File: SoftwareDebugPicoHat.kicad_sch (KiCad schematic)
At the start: 14 parts, among them J1 35362-0950, J2 Conn_Coaxial, J3 USB_C_Receptacle_USB2.0_14P, J4 Conn_Coaxial, J5 Conn_01x04_Pin, U1 RFM98PW, U3 LORA1280F27-TCXO

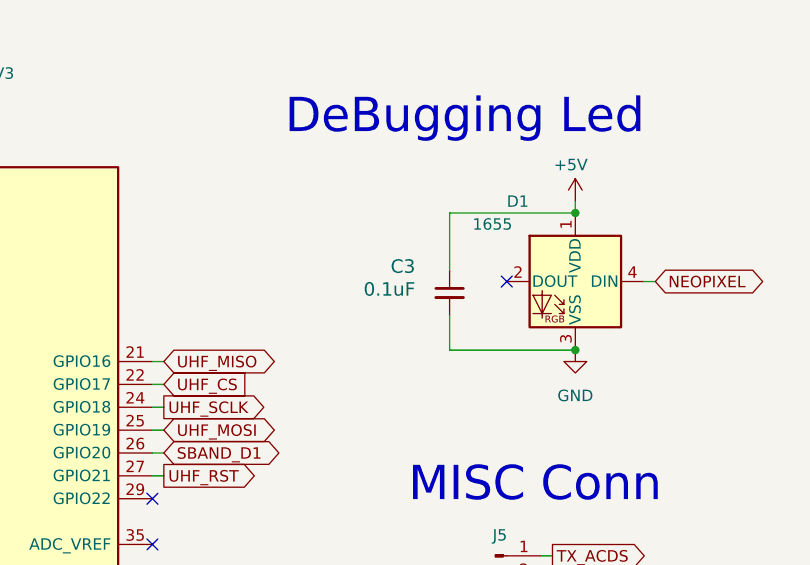
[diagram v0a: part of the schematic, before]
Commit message: Removed UBC and TCXO-EN Pullup resistor
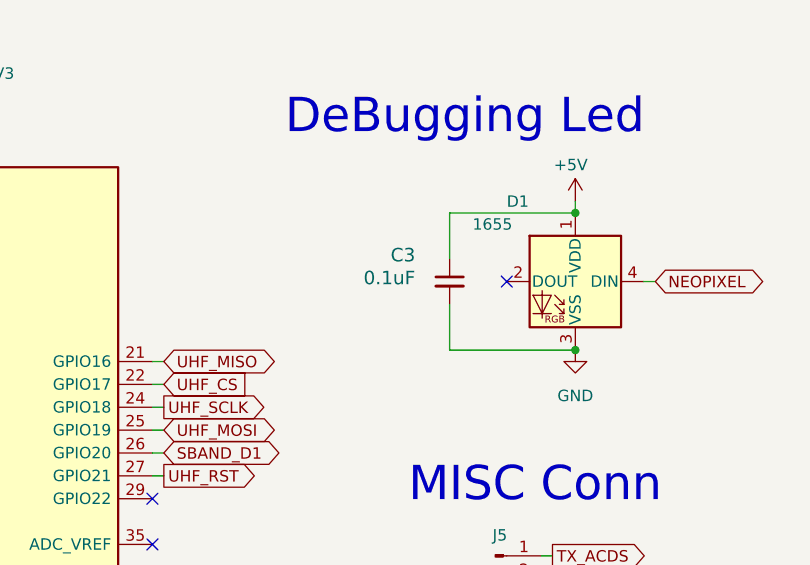
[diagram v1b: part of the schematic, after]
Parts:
- R1, R2: footprint (none) -> Resistor_SMD:R_0603_1608Metric
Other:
- moved on the sheet: C3
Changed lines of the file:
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@@
 	(wire
 		(pts
-			(xy 111.76 46.99) (xy 111.76 50.8)
+			(xy 111.76 45.72) (xy 111.76 50.8)
 		)
 		(stroke
@@
 	(wire
 		(pts
-			(xy 111.76 35.56) (xy 111.76 41.91)
+			(xy 111.76 35.56) (xy 111.76 40.64)
 		)
 		(stroke
@@
 	(symbol
 		(lib_id "Device:C_Small")
-		(at 111.76 44.45 0)
+		(at 111.76 43.18 0)
 		(unit 1)
 		(exclude_from_sim no)
@@
 		(dnp no)
 		(property "Reference" "C3"
-			(at 107.95 40.64 0)
+			(at 107.95 39.37 0)
 			(effects
 				(font
@@
 		)
 		(property "Value" "0.1uF"
-			(at 107.95 43.18 0)
+			(at 107.95 41.91 0)
 			(effects
 				(font
@@
 		)
 		(property "Footprint" "Capacitor_SMD:C_0603_1608Metric"
-			(at 111.76 44.45 0)
+			(at 111.76 43.18 0)
 			(effects
 				(font
@@
 		)
 		(property "Datasheet" "~"
-			(at 111.76 44.45 0)
+			(at 111.76 43.18 0)
 			(effects
 				(font
@@
 		)
 		(property "Description" "Unpolarized capacitor, small symbol"
-			(at 111.76 44.45 0)
+			(at 111.76 43.18 0)
 			(effects
 				(font
@@
 			)
 		)
-		(property "Footprint" ""
+		(property "Footprint" "Resistor_SMD:R_0603_1608Metric"
 			(at 55.88 135.89 0)
 			(effects
@@
 			)
 		)
-		(property "Footprint" ""
+		(property "Footprint" "Resistor_SMD:R_0603_1608Metric"
 			(at 59.69 133.35 0)
 			(effects

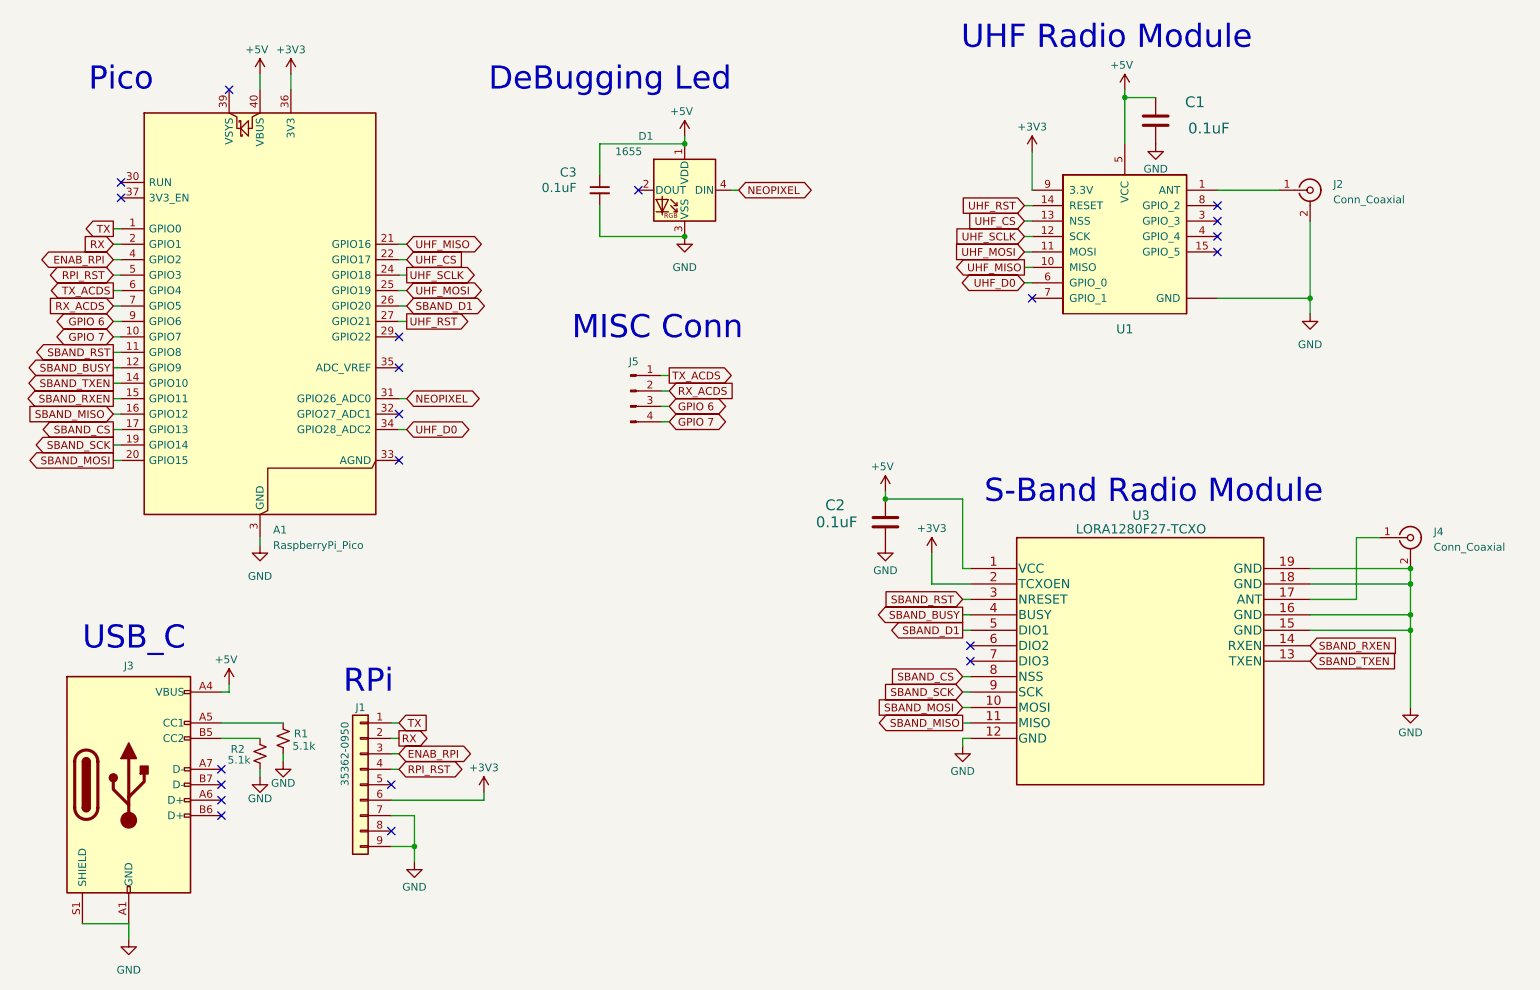
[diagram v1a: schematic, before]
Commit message: FIxed Caps
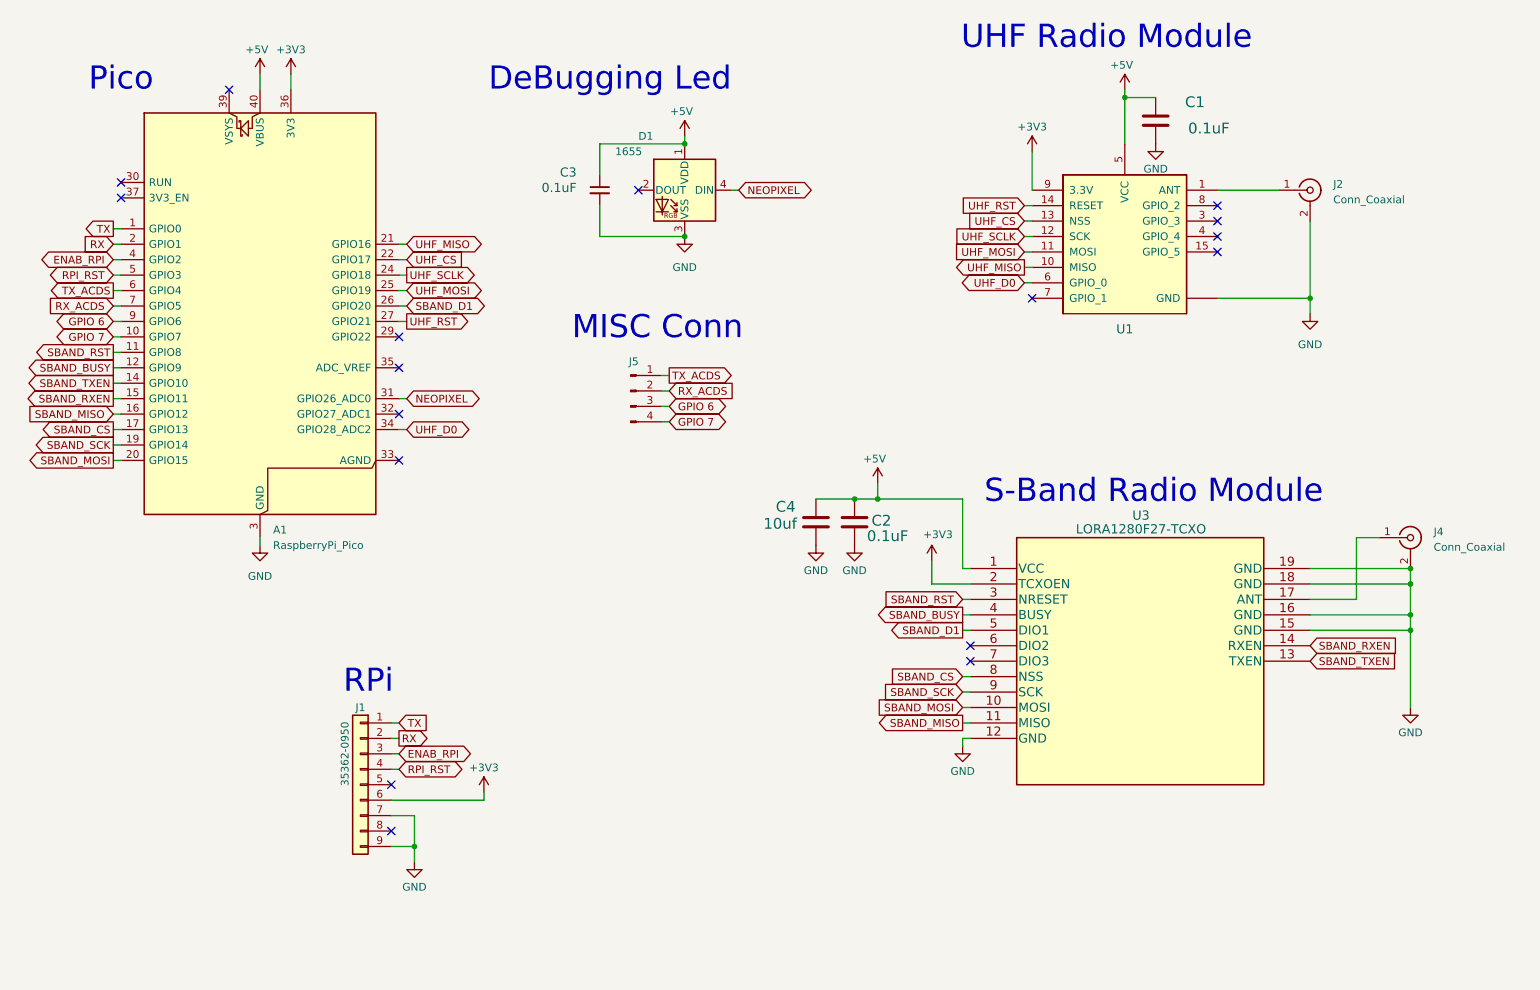
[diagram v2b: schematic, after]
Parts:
- removed J3: USB_C_Receptacle_USB2.0_14P, ssi_connector:USB_C_Receptacle_XKB_U262-161N-4BVC11, symbol Connector:USB_C_Receptacle_USB2.0_14P
- removed R1, R2: 5.1k, Resistor_SMD:R_0603_1608Metric, symbol Device:R_Small_US
- added C4: 10uf, Capacitor_SMD:C_0603_1608Metric, symbol Device:C
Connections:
- net +5V: now also C4.1
- net GND: now also C4.2
- no-connect marks 21 -> 17
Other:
- note removed: "USB_C"
- moved on the sheet: C2
